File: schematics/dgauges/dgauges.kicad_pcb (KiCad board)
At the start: 2 copper layers, 116 x 53.9 mm, 21 parts, among them J1 Conn_01x05_Female, U1 74HC595N, U2 74HC595N, U3 74HC595N, U4 74HC595N, U5 74HC595N

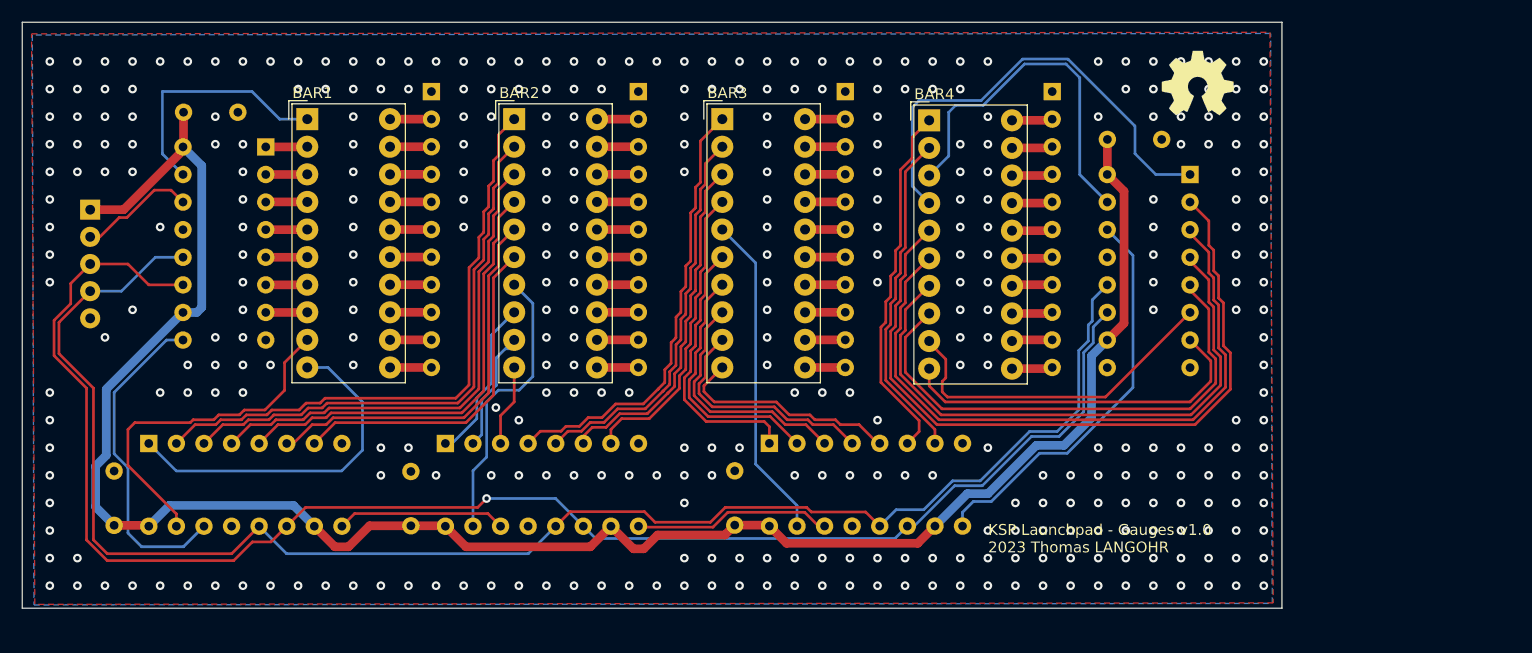
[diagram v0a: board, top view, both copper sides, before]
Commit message: SCH: dgauge => ust proper JST connector for J1
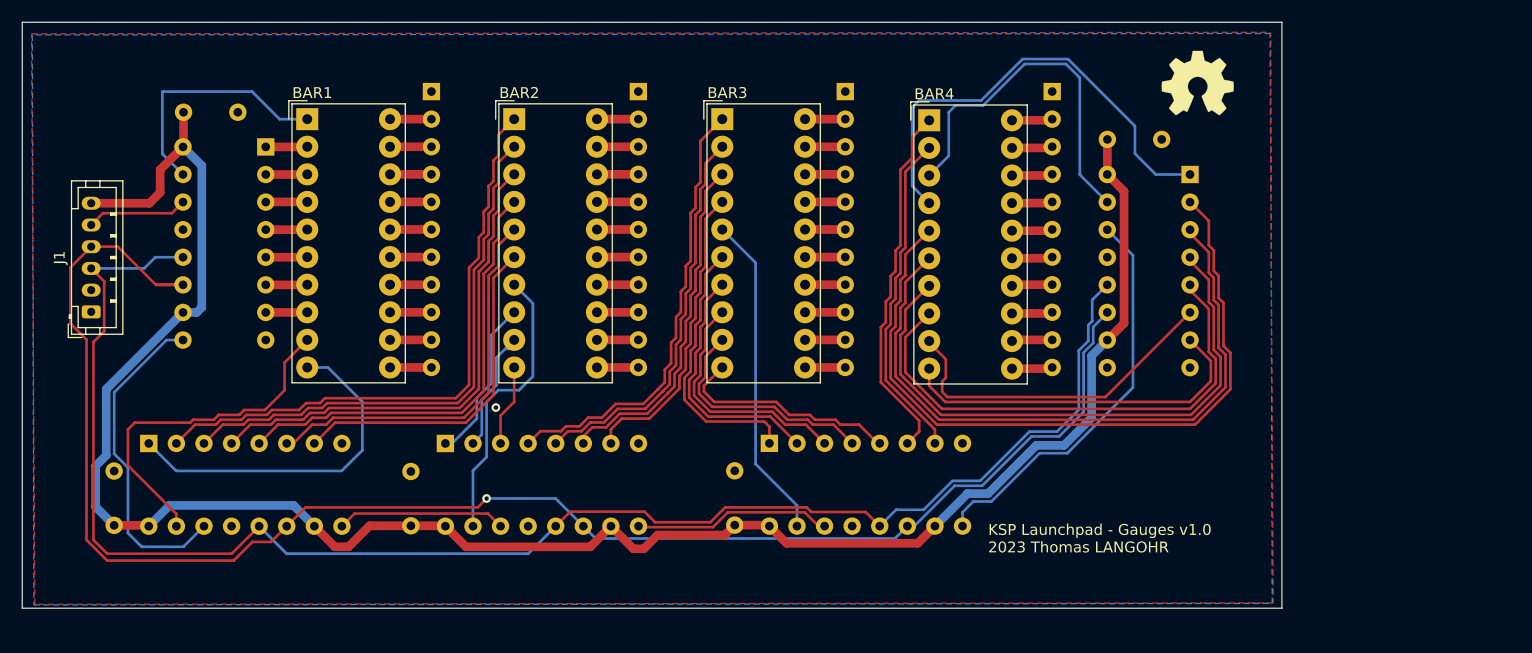
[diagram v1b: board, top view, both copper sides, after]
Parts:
- J1: value Conn_01x05_Female -> Conn_01x06_Socket; footprint Connectors_JST:JST_EH_B05B-EH-A_05x2.50mm_Straight -> Connector_JST:JST_PH_B6B-PH-K_1x06_P2.00mm_Vertical; moved to F.Cu
- U1, U2, U3, U4, U5: value 74HC595N -> 74HC595
- moved J1 9.41 mm to (100.3, 96.7), turned to 90 degrees
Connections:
- J1 pad 1: +5V -> GND
- J1 pad 2: /DG_DATA -> GND
- J1 pad 3: /DG_CLK -> /~{DG_LATCH}
- J1 pad 4: /~{DG_LATCH} -> /DG_CLK
- J1 pad 5: GND -> /DG_DATA
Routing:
- net /DG_CLK: track 148.1 -> 151.4 mm
- net /DG_DATA: track 10.8 -> 9.32 mm
- net +5V: track 184.2 -> 185.3 mm
- net GND: vias 364 -> 1

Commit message: SCH: DGauges: route serial out to header for daisy-chaining
And add mounting holes
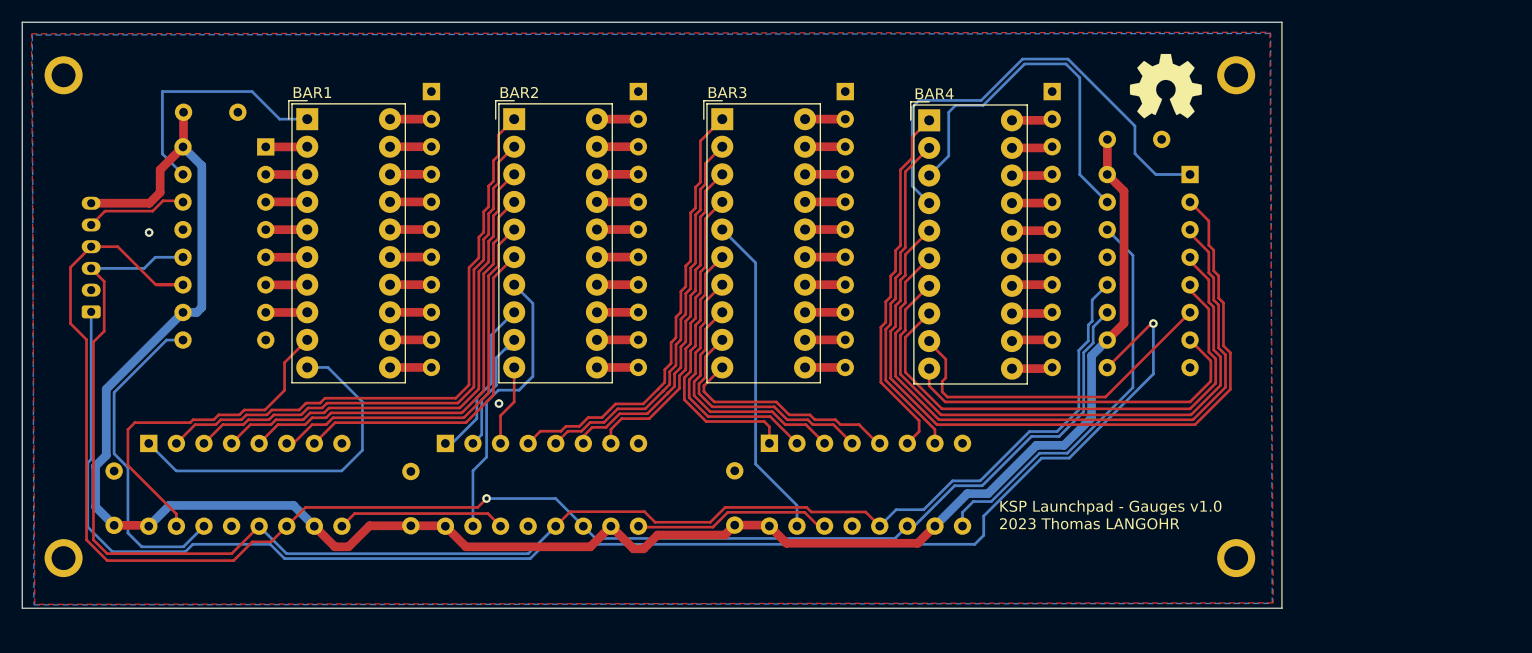
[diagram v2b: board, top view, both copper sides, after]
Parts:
- added H1: MountingHole_Pad, MountingHole:MountingHole_2.2mm_M2_ISO7380_Pad, F.Cu at (97.8, 74.9)
- added H2: MountingHole_Pad, MountingHole:MountingHole_2.2mm_M2_ISO7380_Pad, F.Cu at (205.7, 74.9)
- added H3: MountingHole_Pad, MountingHole:MountingHole_2.2mm_M2_ISO7380_Pad, F.Cu at (97.8, 119.4)
- added H4: MountingHole_Pad, MountingHole:MountingHole_2.2mm_M2_ISO7380_Pad, F.Cu at (205.7, 119.4)
- J1: moved to B.Cu
- moved REF** 2.94 mm to (199.3, 75.9) (x2)
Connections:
- J1 pad 1: GND -> Net-(J1-Pin_1)
- U1 pad 13: GND -> unconnected-(U1-~{OE}-Pad13)
- U4 pad 9: unconnected-(U4-QH'-Pad9) -> Net-(J1-Pin_1)
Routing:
- net Net-(J1-Pin_1): track 0.00 -> 138.5 mm, vias 0 -> 1
- net GND: vias 1 -> 2

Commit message: SCH: tune mounting holes
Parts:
- moved H1 1.27 mm to (97.8, 73.7)
- moved H2 1.27 mm to (205.7, 73.7)
- moved H3 1.27 mm to (97.8, 120.7)
- moved H4 1.27 mm to (205.7, 120.7)
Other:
- board size 116 x 53.9 mm -> 116 x 54.6 mm
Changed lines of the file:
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@@
   (net 91 "Net-(U5-QH)")
   (footprint "MountingHole:MountingHole_2.2mm_M2_ISO7380_Pad" (layer "F.Cu")
-    (at 205.74 74.93)
+    (at 205.74 73.66)
     (descr "Mounting Hole 2.2mm, M2, ISO7380")
     (tags "mounting hole 2.2mm m2 iso7380")
@@
   )
   (footprint "MountingHole:MountingHole_2.2mm_M2_ISO7380_Pad" (layer "F.Cu")
-    (at 97.79 74.93)
+    (at 97.79 73.66)
     (descr "Mounting Hole 2.2mm, M2, ISO7380")
     (tags "mounting hole 2.2mm m2 iso7380")
@@
   )
   (footprint "MountingHole:MountingHole_2.2mm_M2_ISO7380_Pad" (layer "F.Cu")
-    (at 205.74 119.38)
+    (at 205.74 120.65)
     (descr "Mounting Hole 2.2mm, M2, ISO7380")
     (tags "mounting hole 2.2mm m2 iso7380")
@@
   )
   (footprint "MountingHole:MountingHole_2.2mm_M2_ISO7380_Pad" (layer "F.Cu")
-    (at 97.79 119.38)
+    (at 97.79 120.65)
     (descr "Mounting Hole 2.2mm, M2, ISO7380")
     (tags "mounting hole 2.2mm m2 iso7380")
@@
     )
   )
-  (gr_rect (start 93.985 70.05) (end 209.955 123.995)
+  (gr_rect (start 93.985 70.05) (end 209.955 124.63)
     (stroke (width 0.1) (type default)) (fill none) (layer "Edge.Cuts"))
   (gr_text "KSP Launchpad - Gauges v1.0\n2023 Thomas LANGOHR" (at 207.645 116.84) (layer "B.SilkS")

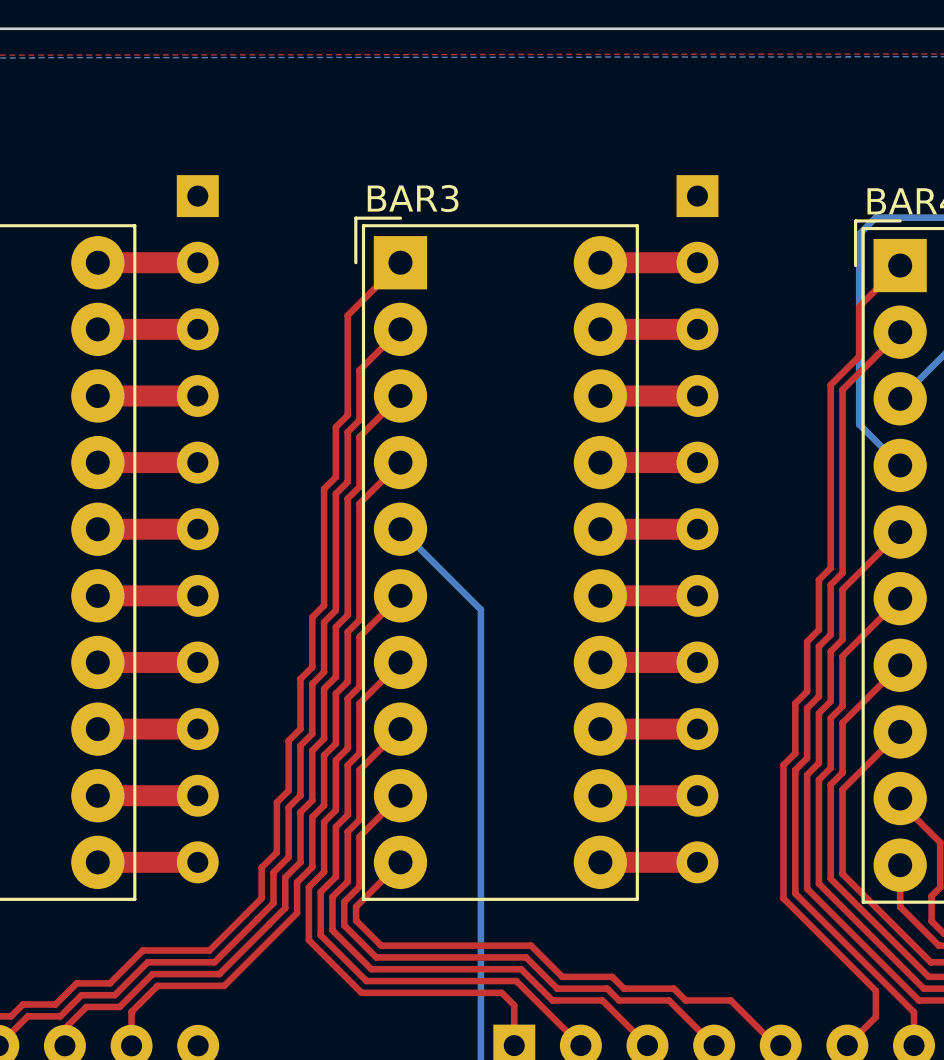
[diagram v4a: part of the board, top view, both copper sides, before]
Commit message: SCH: dgauges=> set res. values to get similar brightness on all bars
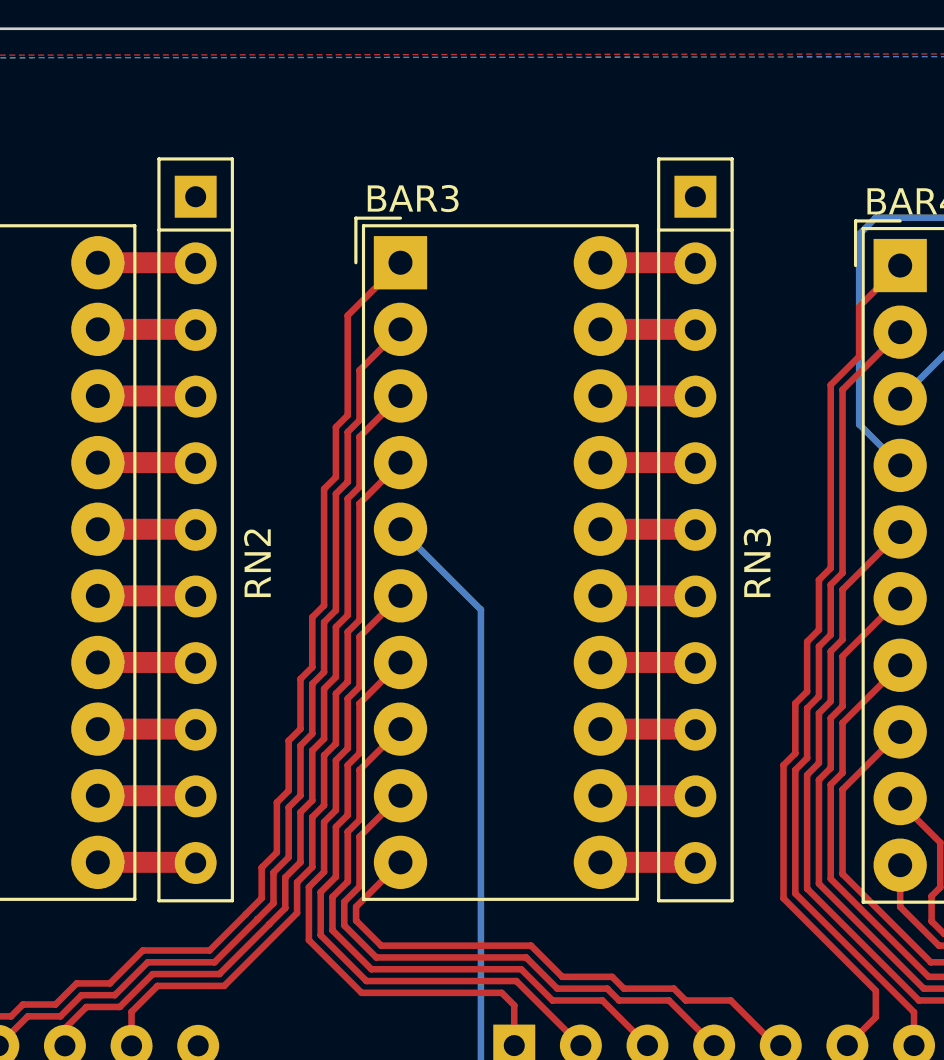
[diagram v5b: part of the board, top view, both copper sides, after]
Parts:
- RN1: value R470 -> 1k
- RN2: value R470 -> R330; moved to F.Cu
- RN3: value R470 -> 1k; moved to F.Cu
- RN4: value R470 -> R330
- moved RN3 0.08 mm to (169.7, 76.5)
- moved RN2 0.08 mm to (150.6, 76.5)
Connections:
- U1 pad 13: unconnected-(U1-~{OE}-Pad13) -> GND

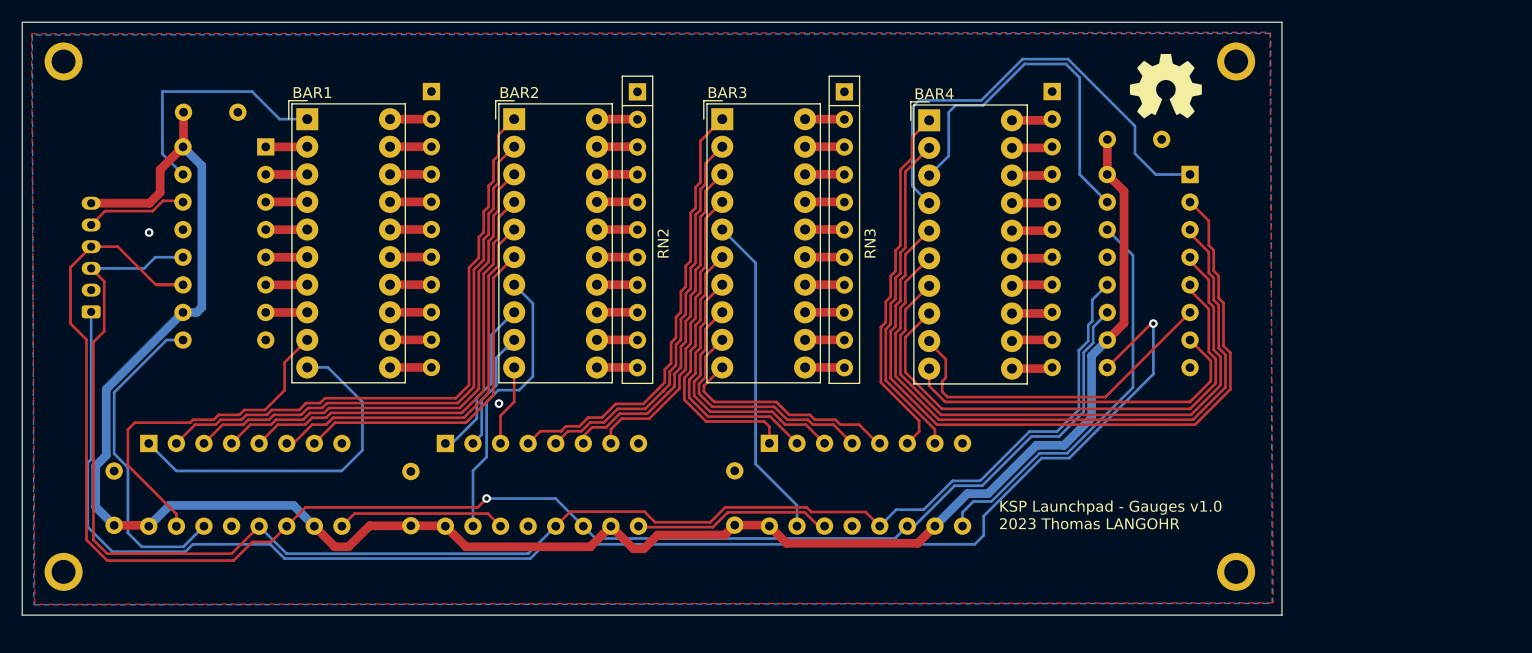
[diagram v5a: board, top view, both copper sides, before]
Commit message: Sch: gauges: add one for xenon
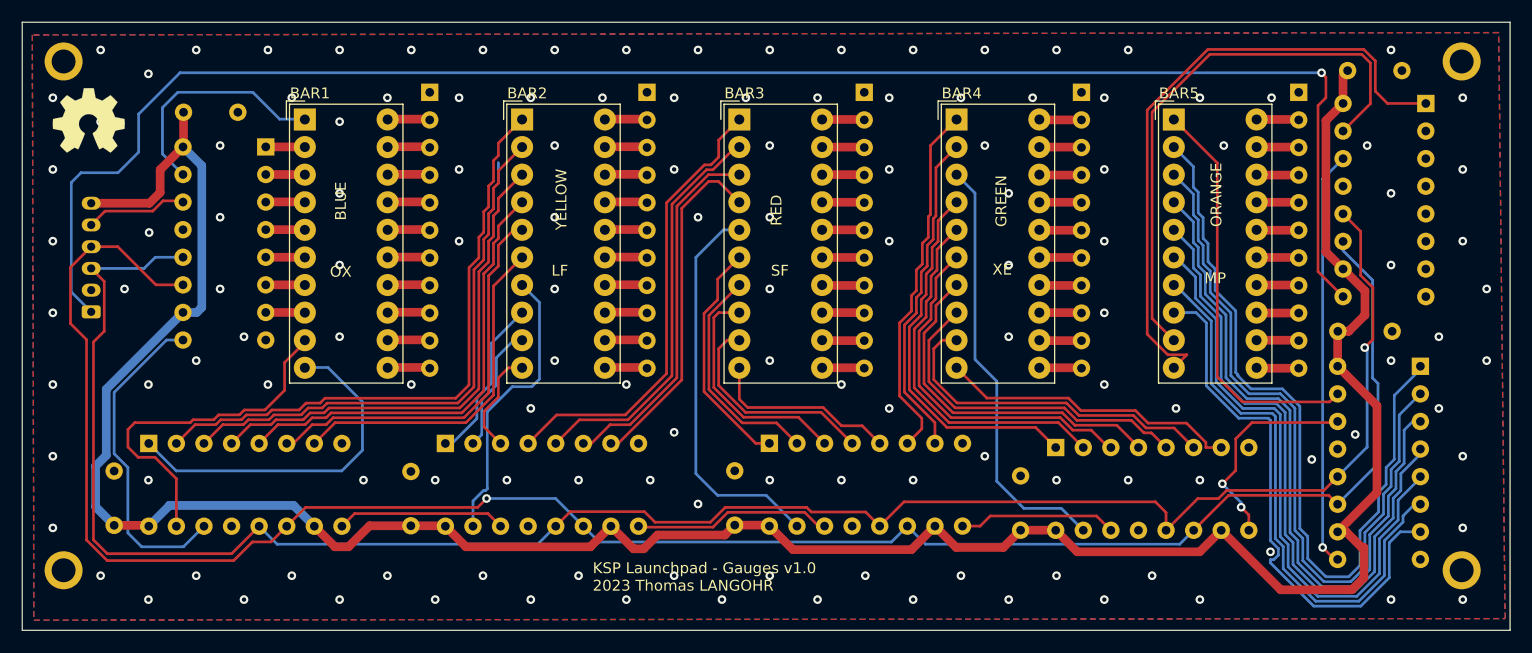
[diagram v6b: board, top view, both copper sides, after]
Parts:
- added BAR5: EADLBA10OA1, Display:HDSP-4832, F.Cu at (200.0, 79.0)
- added C6: 0.1 µf, Capacitor_THT:C_Disc_D4.3mm_W1.9mm_P5.00mm, B.Cu at (215.1, 98.5)
- added C7: 0.1 µf, Capacitor_THT:C_Disc_D4.3mm_W1.9mm_P5.00mm, B.Cu at (216.0, 74.5)
- added RN5: R330, Resistor_THT:R_Array_SIP11, B.Cu at (211.5, 76.5)
- added U6: 74HC595, Package_DIP:DIP-16_W7.62mm, B.Cu at (222.7, 101.7)
- added U7: 74HC595, Package_DIP:DIP-16_W7.62mm, B.Cu at (223.2, 77.5)
- RN2, RN3: moved to B.Cu
- moved REF** 99.2 mm to (100.1, 79.1) (x2)
- moved C5 36.9 mm to (185.9, 116.8), turned to 90 degrees
- moved U4 28.0 mm to (189.1, 109.2), turned to -90 degrees
- moved H4 20.8 mm to (226.5, 120.5)
- moved H2 20.8 mm to (226.5, 73.7)
- moved RN4 2.70 mm to (191.5, 76.5)
- moved BAR4 2.52 mm to (180.0, 79.0)
- moved RN3 1.83 mm to (171.5, 76.5)
- moved BAR3 1.57 mm to (160.0, 79.0)
- moved RN2 0.88 mm to (151.5, 76.5)
- moved BAR2 0.73 mm to (140.0, 79.0)
- moved BAR1 0.22 mm to (120.0, 79.0)
- moved RN1 0.17 mm to (131.5, 76.5)
- moved H3 0.15 mm to (97.8, 120.5)
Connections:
- J1 pad 1: Net-(J1-Pin_1) -> /SER_OUT
- U4 pad 9: Net-(J1-Pin_1) -> Net-(U4-QH')
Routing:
- net /SER_OUT: track 0.00 -> 156.0 mm, vias 0 -> 1
- net Net-(J1-Pin_1): track 138.5 -> 0.00 mm, vias 1 -> 0
- net Net-(U6-QB): track 0.00 -> 71.3 mm
- net Net-(U6-QC): track 0.00 -> 67.3 mm
- net Net-(U6-QD): track 0.00 -> 63.8 mm
- net Net-(U6-QE): track 0.00 -> 59.4 mm
- net Net-(U7-QB): track 0.00 -> 58.4 mm
- net Net-(U6-QF): track 0.00 -> 55.5 mm
- net +5V: track 185.3 -> 240.3 mm
- net Net-(U6-QG): track 0.00 -> 51.9 mm
- net Net-(U7-QA): track 0.00 -> 51.8 mm
- net Net-(U6-QH): track 0.00 -> 50.5 mm
- net Net-(U6-QH'): track 0.00 -> 38.4 mm, vias 0 -> 1
- net /~{DG_LATCH}: track 148.4 -> 186.4 mm, vias 0 -> 1
- net Net-(U6-QA): track 0.00 -> 37.7 mm
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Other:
- board size 116 x 54.6 mm -> 137 x 56 mm
- board text added: "BLUE"
- board text added: "GREEN"
- board text added: "LF"
- board text added: "MP"
- board text added: "ORANGE"
- board text added: "OX"
- board text added: "RED"
- board text added: "SF"
- board text added: "XE"
- board text added: "YELLOW"

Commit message: panels: gauges=> aligned mounting holes
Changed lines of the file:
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@@
     (fp_line (start 11.95 1.7) (end -1.95 1.7)
       (stroke (width 0.1) (type solid)) (layer "B.Fab"))
-    (pad "1" thru_hole roundrect (at 0 0 90) (size 1.2 1.75) (drill 0.75) (layers "*.Cu" "*.Mask") (roundrect_rratio 0.208333)
+    (pad "1" thru_hole roundrect (at 0 0 90) (size 1.2 1.75) (drill 0.75) (layers "*.Cu" "*.Mask") (roundrect_rratio 0.2083333333)
       (net 110 "/SER_OUT") (pinfunction "Pin_1") (pintype "passive"))
     (pad "2" thru_hole oval (at 2 0 90) (size 1.2 1.75) (drill 0.75) (layers "*.Cu" "*.Mask")
